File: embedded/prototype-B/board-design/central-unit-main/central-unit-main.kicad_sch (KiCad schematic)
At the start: 0 parts

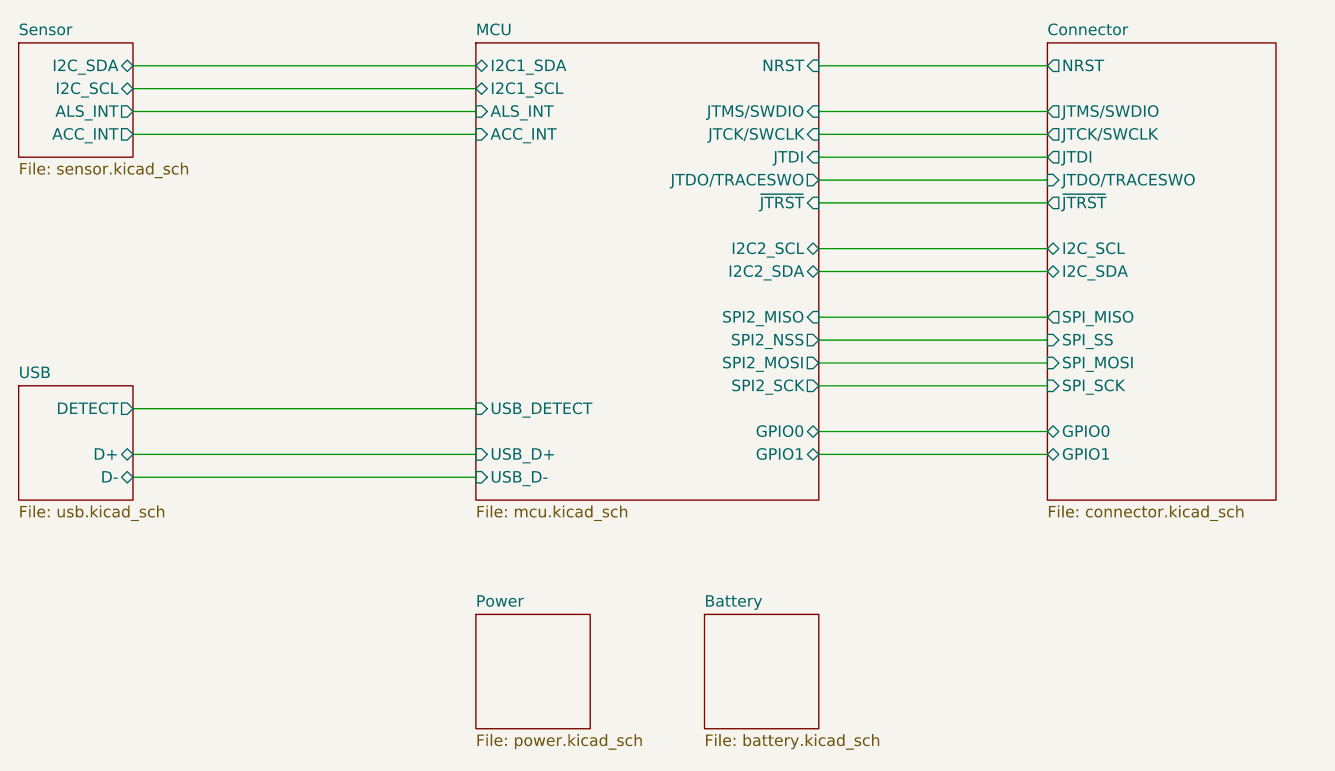
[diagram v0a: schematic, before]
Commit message: [Central unit]
Integrated the LED driver into the cetral unit board.

Signed-off-by: Nicolae-Andrei Prodan <vasilenicolaeandrei@gmail.com>
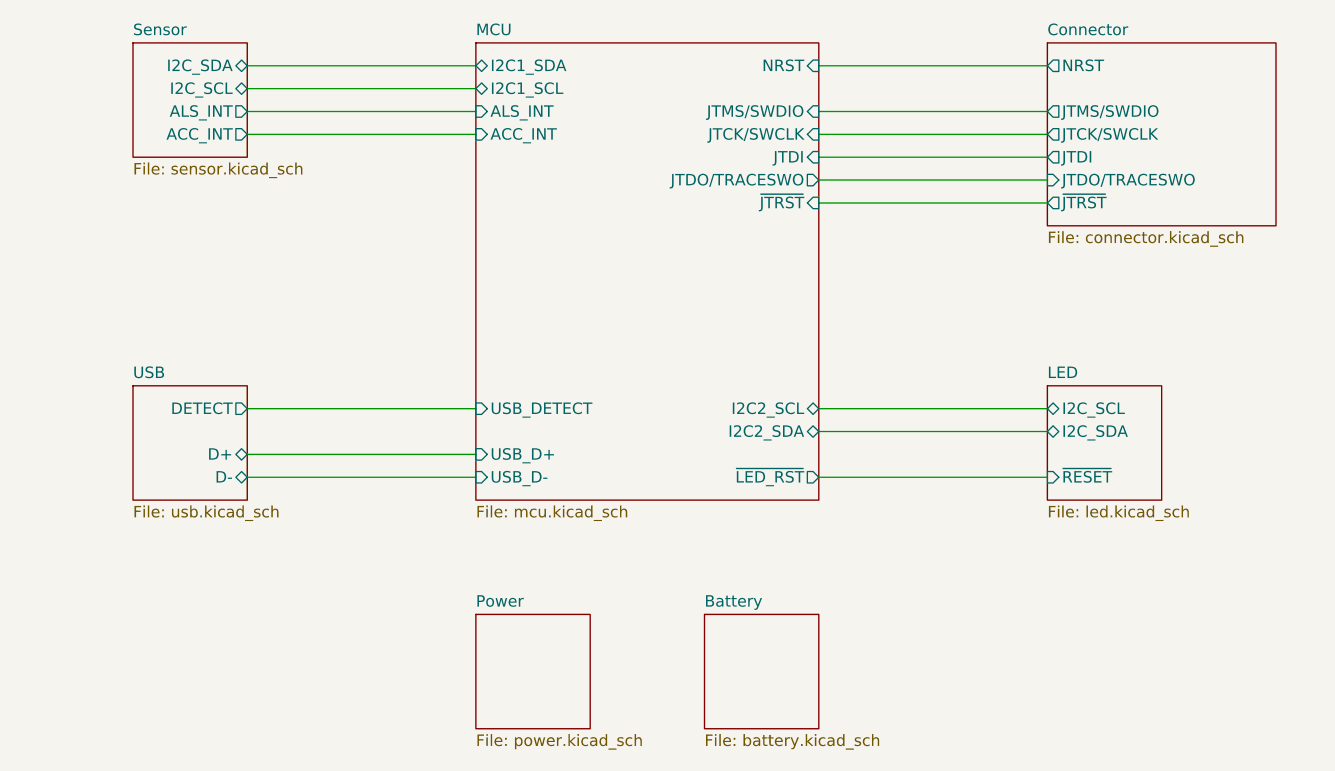
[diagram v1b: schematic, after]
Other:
- added sheet LED (led.kicad_sch)
- sheet Connector ports: added none; removed GPIO0, GPIO1, I2C_SCL, I2C_SDA, SPI_MISO, SPI_MOSI, SPI_SCK, SPI_SS
- sheet MCU ports: added ~{LED_RST}; removed GPIO0, GPIO1, SPI2_MISO, SPI2_MOSI, SPI2_NSS, SPI2_SCK
